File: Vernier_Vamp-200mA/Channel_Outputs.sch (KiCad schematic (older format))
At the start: 87 parts, among them Q3 2SC5566, Q4 2SA2013, Q5 2SC5566, Q6 2SA2013, Q7 2SC5566, Q8 2SA2013, U12 OPA2277, U13 OPA2277, U14 OPA2277

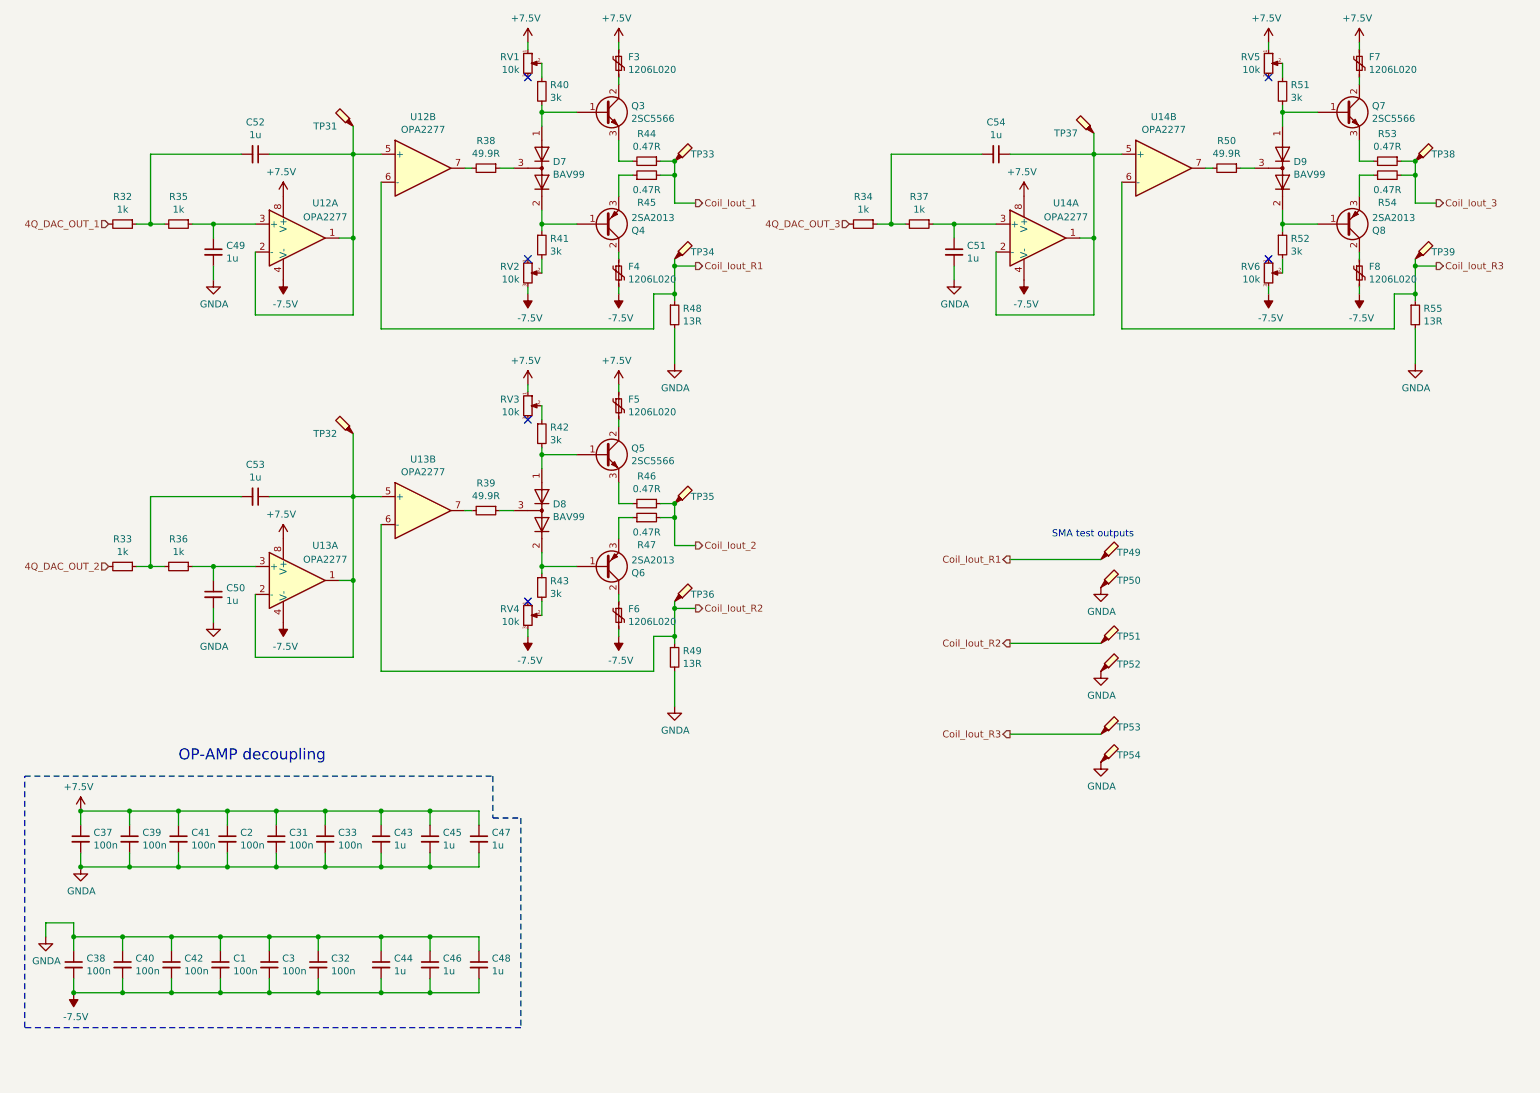
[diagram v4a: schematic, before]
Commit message: Addition of test points onto the bias circuitry
-Addition of test points onto the bias circuitry (HCCD)
-Silkscreen update (LCCD)
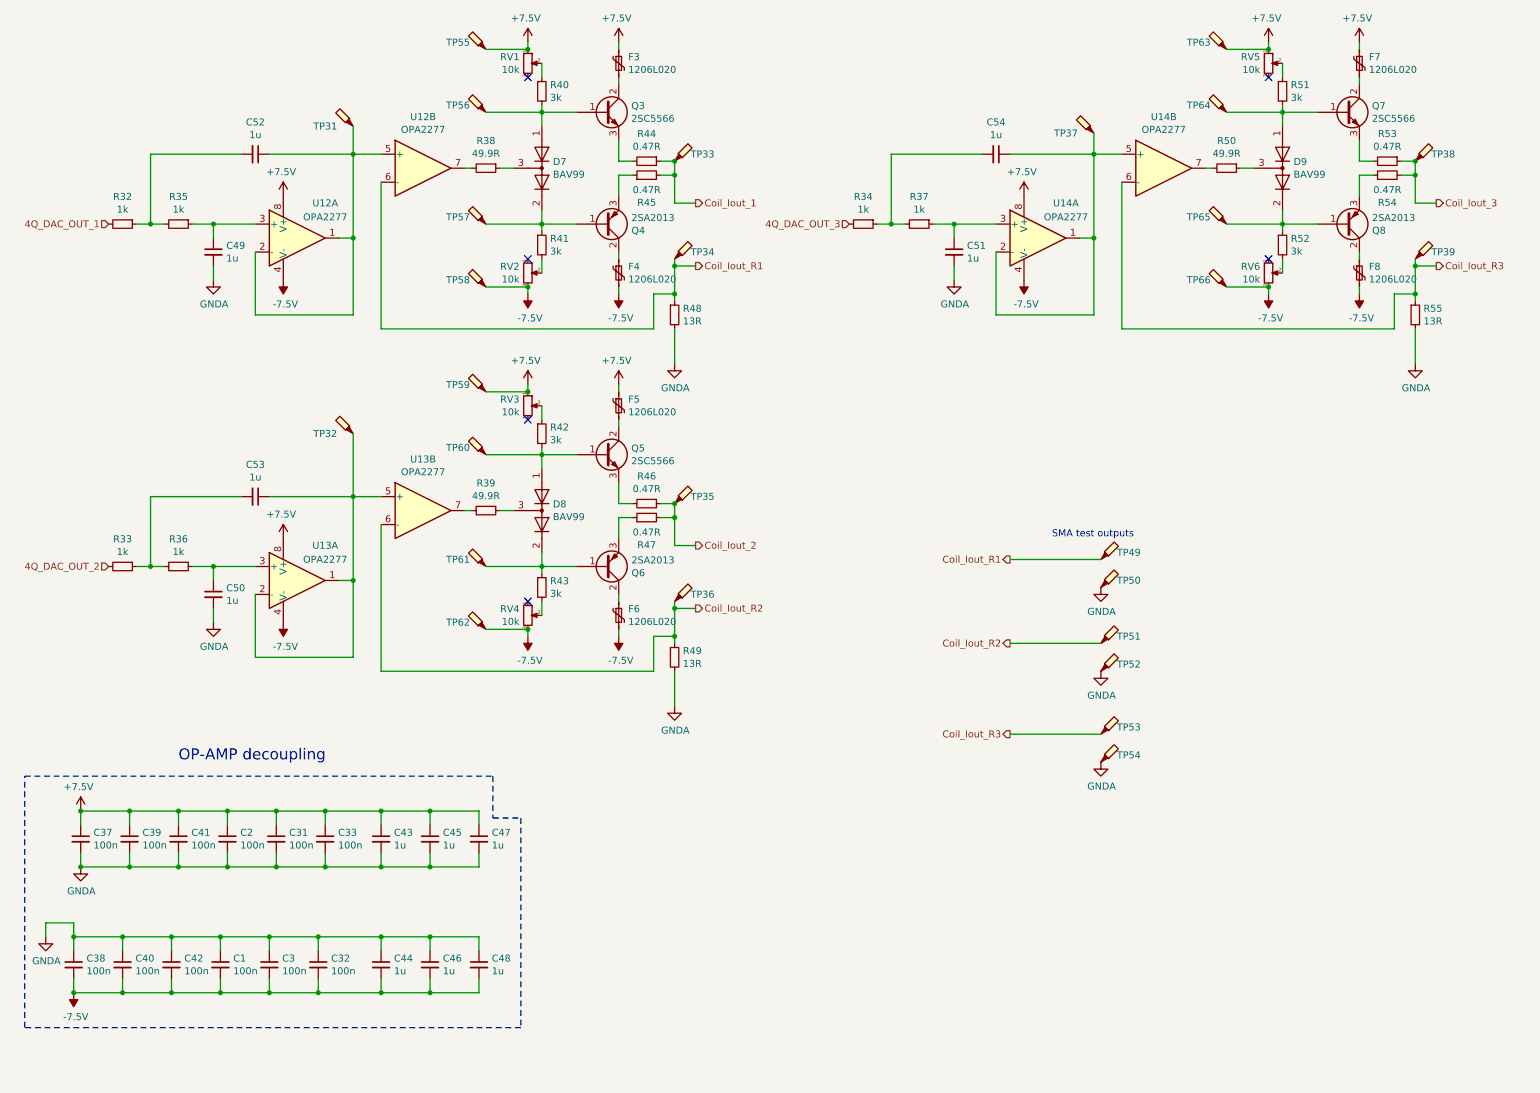
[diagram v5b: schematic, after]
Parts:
- added TP55, TP56, TP57, TP58, TP59, TP60, TP61, TP62, TP63, TP64, TP65, TP66: TestPoint_Probe, TestPoint:TestPoint_Pad_D1.0mm, symbol Connector:TestPoint_Probe
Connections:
- net +7V5: now also TP55.1, TP59.1, TP63.1
- net -7V5: now also TP58.1, TP62.1, TP66.1
- net at D8.2 (A), Q6.1, R43.1: now also TP61.1
- net at D8.1 (K), Q5.1, R42.2: now also TP60.1
- net at D7.2 (A), Q4.1, R41.1: now also TP57.1
- net at D7.1 (K), Q3.1, R40.2: now also TP56.1
- net at D9.2 (A), Q8.1, R52.1: now also TP65.1
- net at D9.1 (K), Q7.1, R51.2: now also TP64.1
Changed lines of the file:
@@
 Wire Wire Line
 	7550 5650 8200 5650
+$Comp
+L Connector:TestPoint_Probe TP?
+U 1 1 60A878FD
+P 3800 750
+AR Path="/5E1DEB8C/60A878FD" Ref="TP?"  Part="1"
+AR Path="/5E1E279E/60A878FD" Ref="TP55"  Part="1"
+F 0 "TP55" H 4000 800 50  0000 C CNN
+F 1 "TestPoint_Probe" V 3999 805 50  0001 C CNN
+F 2 "TestPoint:TestPoint_Pad_D1.0mm" H 4000 750 50  0001 C CNN
+F 3 "~" H 4000 750 50  0001 C CNN
+	1    3800 750
+	-1   0    0    -1
+$EndComp
+Wire Wire Line
+	3800 750  4100 750
+Connection ~ 4100 750
+$Comp
+L Connector:TestPoint_Probe TP?
+U 1 1 60AAAEC5
+P 3800 1200
+AR Path="/5E1DEB8C/60AAAEC5" Ref="TP?"  Part="1"
+AR Path="/5E1E279E/60AAAEC5" Ref="TP56"  Part="1"
+F 0 "TP56" H 4000 1250 50  0000 C CNN
+F 1 "TestPoint_Probe" V 3999 1255 50  0001 C CNN
+F 2 "TestPoint:TestPoint_Pad_D1.0mm" H 4000 1200 50  0001 C CNN
+F 3 "~" H 4000 1200 50  0001 C CNN
+	1    3800 1200
+	-1   0    0    -1
+$EndComp
+Wire Wire Line
+	3800 1200 4200 1200
+$Comp
+L Connector:TestPoint_Probe TP?
+U 1 1 60ADBAA7
+P 3800 2450
+AR Path="/5E1DEB8C/60ADBAA7" Ref="TP?"  Part="1"
+AR Path="/5E1E279E/60ADBAA7" Ref="TP58"  Part="1"
+F 0 "TP58" H 4000 2500 50  0000 C CNN
+F 1 "TestPoint_Probe" V 3999 2505 50  0001 C CNN
+F 2 "TestPoint:TestPoint_Pad_D1.0mm" H 4000 2450 50  0001 C CNN
+F 3 "~" H 4000 2450 50  0001 C CNN
+	1    3800 2450
+	-1   0    0    -1
+$EndComp
+Wire Wire Line
+	3800 2450 4100 2450
+$Comp
+L Connector:TestPoint_Probe TP?
+U 1 1 60ADBAAE
+P 3800 2000
+AR Path="/5E1DEB8C/60ADBAAE" Ref="TP?"  Part="1"
+AR Path="/5E1E279E/60ADBAAE" Ref="TP57"  Part="1"
+F 0 "TP57" H 4000 2050 50  0000 C CNN
+F 1 "TestPoint_Probe" V 3999 2055 50  0001 C CNN
+F 2 "TestPoint:TestPoint_Pad_D1.0mm" H 4000 2000 50  0001 C CNN
+F 3 "~" H 4000 2000 50  0001 C CNN
+	1    3800 2000
+	-1   0    0    -1
+$EndComp
+Wire Wire Line
+	3800 2000 4200 2000
+Connection ~ 4100 2450
+$Comp
+L Connector:TestPoint_Probe TP?
+U 1 1 60B01273
+P 3800 3200
+AR Path="/5E1DEB8C/60B01273" Ref="TP?"  Part="1"
+AR Path="/5E1E279E/60B01273" Ref="TP59"  Part="1"
+F 0 "TP59" H 4000 3250 50  0000 C CNN
+F 1 "TestPoint_Probe" V 3999 3255 50  0001 C CNN
+F 2 "TestPoint:TestPoint_Pad_D1.0mm" H 4000 3200 50  0001 C CNN
+F 3 "~" H 4000 3200 50  0001 C CNN
+	1    3800 3200
+	-1   0    0    -1
+$EndComp
+$Comp
+L Connector:TestPoint_Probe TP?
+U 1 1 60B0127A
+P 3800 3650
+AR Path="/5E1DEB8C/60B0127A" Ref="TP?"  Part="1"
+AR Path="/5E1E279E/60B0127A" Ref="TP60"  Part="1"
+F 0 "TP60" H 4000 3700 50  0000 C CNN
+F 1 "TestPoint_Probe" V 3999 3705 50  0001 C CNN
+F 2 "TestPoint:TestPoint_Pad_D1.0mm" H 4000 3650 50  0001 C CNN
+F 3 "~" H 4000 3650 50  0001 C CNN
+	1    3800 3650
+	-1   0    0    -1
+$EndComp
+Wire Wire Line
+	3800 3650 4200 3650
+Connection ~ 4100 3200
+Wire Wire Line
+	3800 3200 4100 3200
+$Comp
+L Connector:TestPoint_Probe TP?
+U 1 1 60B2A31C
+P 3800 4900
+AR Path="/5E1DEB8C/60B2A31C" Ref="TP?"  Part="1"
+AR Path="/5E1E279E/60B2A31C" Ref="TP62"  Part="1"
+F 0 "TP62" H 4000 4950 50  0000 C CNN
+F 1 "TestPoint_Probe" V 3999 4955 50  0001 C CNN
+F 2 "TestPoint:TestPoint_Pad_D1.0mm" H 4000 4900 50  0001 C CNN
+F 3 "~" H 4000 4900 50  0001 C CNN
+	1    3800 4900
+	-1   0    0    -1
+$EndComp
+Wire Wire Line
+	3800 4900 4100 4900
+$Comp
+L Connector:TestPoint_Probe TP?
+U 1 1 60B2A323
+P 3800 4450
+AR Path="/5E1DEB8C/60B2A323" Ref="TP?"  Part="1"
+AR Path="/5E1E279E/60B2A323" Ref="TP61"  Part="1"
+F 0 "TP61" H 4000 4500 50  0000 C CNN
+F 1 "TestPoint_Probe" V 3999 4505 50  0001 C CNN
+F 2 "TestPoint:TestPoint_Pad_D1.0mm" H 4000 4450 50  0001 C CNN
+F 3 "~" H 4000 4450 50  0001 C CNN
+	1    3800 4450
+	-1   0    0    -1
+$EndComp
+Wire Wire Line
+	3800 4450 4200 4450
+$Comp
+L Connector:TestPoint_Probe TP?
+U 1 1 60B381C4
+P 9100 2450
+AR Path="/5E1DEB8C/60B381C4" Ref="TP?"  Part="1"
+AR Path="/5E1E279E/60B381C4" Ref="TP66"  Part="1"
+F 0 "TP66" H 9300 2500 50  0000 C CNN
+F 1 "TestPoint_Probe" V 9299 2505 50  0001 C CNN
+F 2 "TestPoint:TestPoint_Pad_D1.0mm" H 9300 2450 50  0001 C CNN
+F 3 "~" H 9300 2450 50  0001 C CNN
+	1    9100 2450
+	-1   0    0    -1
+$EndComp
+$Comp
+L Connector:TestPoint_Probe TP?
+U 1 1 60B381CB
+P 9100 2000
+AR Path="/5E1DEB8C/60B381CB" Ref="TP?"  Part="1"
+AR Path="/5E1E279E/60B381CB" Ref="TP65"  Part="1"
+F 0 "TP65" H 9300 2050 50  0000 C CNN
+F 1 "TestPoint_Probe" V 9299 2055 50  0001 C CNN
+F 2 "TestPoint:TestPoint_Pad_D1.0mm" H 9300 2000 50  0001 C CNN
+F 3 "~" H 9300 2000 50  0001 C CNN
+	1    9100 2000
+	-1   0    0    -1
+$EndComp
+Wire Wire Line
+	9100 2000 9500 2000
+Wire Wire Line
+	9400 2450 9100 2450
+Connection ~ 9400 2450
+Connection ~ 4100 4900
+$Comp
+L Connector:TestPoint_Probe TP?
+U 1 1 60B6BC89
+P 9100 750
+AR Path="/5E1DEB8C/60B6BC89" Ref="TP?"  Part="1"
+AR Path="/5E1E279E/60B6BC89" Ref="TP63"  Part="1"
+F 0 "TP63" H 9300 800 50  0000 C CNN
+F 1 "TestPoint_Probe" V 9299 805 50  0001 C CNN
+F 2 "TestPoint:TestPoint_Pad_D1.0mm" H 9300 750 50  0001 C CNN
+F 3 "~" H 9300 750 50  0001 C CNN
+	1    9100 750
+	-1   0    0    -1
+$EndComp
+Wire Wire Line
+	9100 750  9400 750
+$Comp
+L Connector:TestPoint_Probe TP?
+U 1 1 60B6BC90
+P 9100 1200
+AR Path="/5E1DEB8C/60B6BC90" Ref="TP?"  Part="1"
+AR Path="/5E1E279E/60B6BC90" Ref="TP64"  Part="1"
+F 0 "TP64" H 9300 1250 50  0000 C CNN
+F 1 "TestPoint_Probe" V 9299 1255 50  0001 C CNN
+F 2 "TestPoint:TestPoint_Pad_D1.0mm" H 9300 1200 50  0001 C CNN
+F 3 "~" H 9300 1200 50  0001 C CNN
+	1    9100 1200
+	-1   0    0    -1
+$EndComp
+Wire Wire Line
+	9100 1200 9500 1200
+Connection ~ 9400 750
 $EndSCHEMATC
